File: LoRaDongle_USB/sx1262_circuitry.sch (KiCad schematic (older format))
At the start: 30 parts

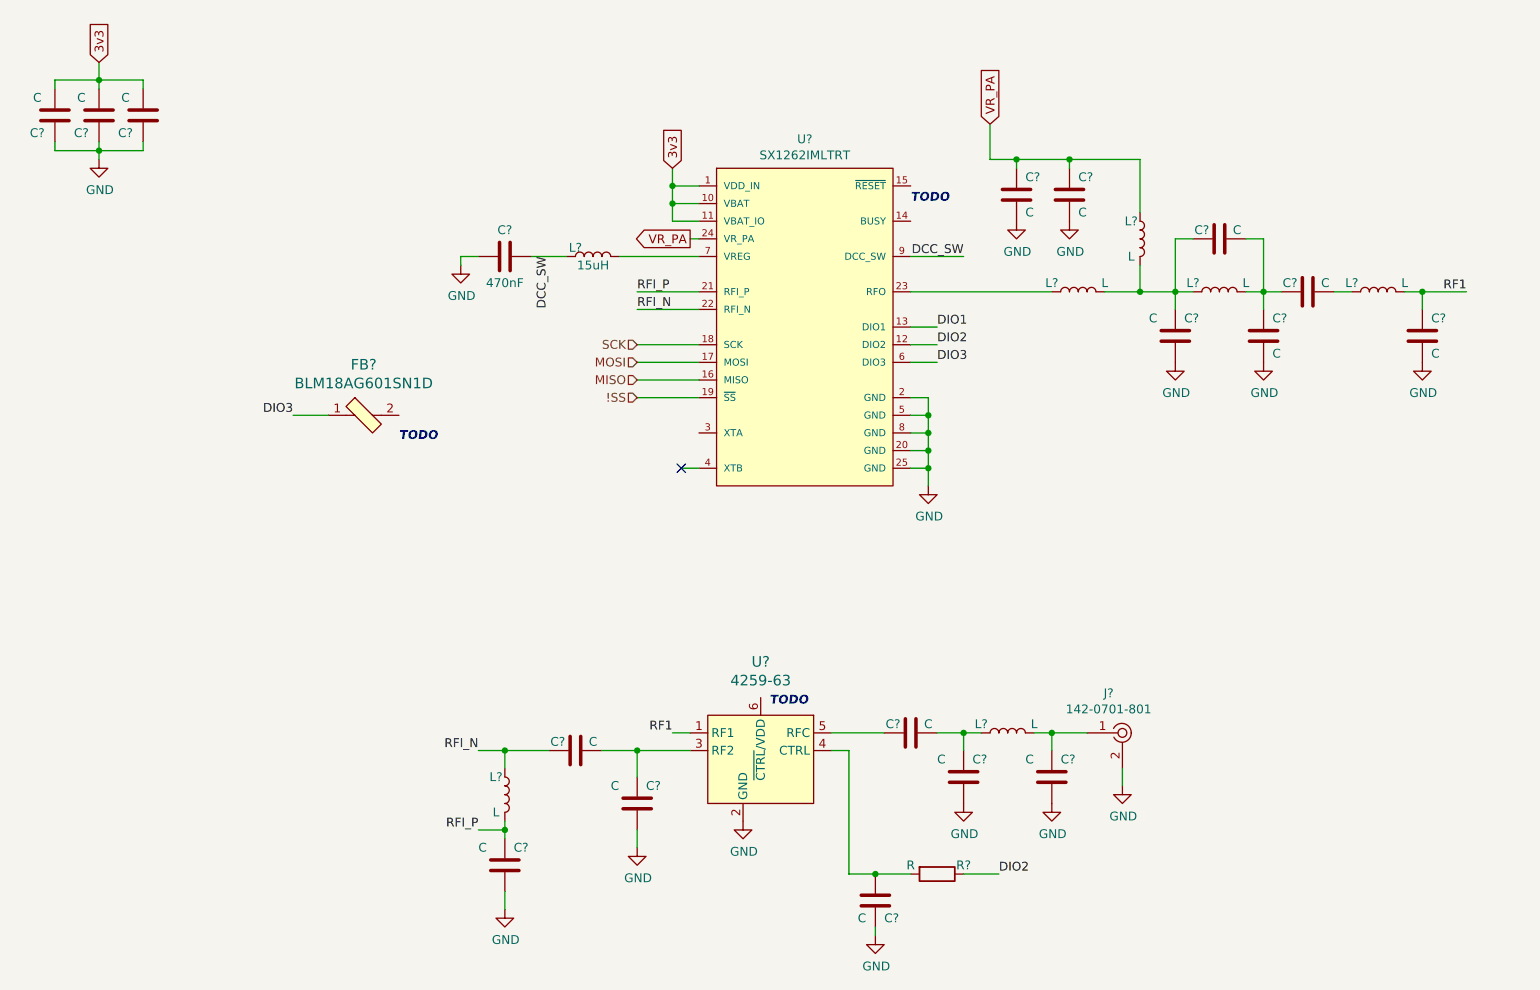
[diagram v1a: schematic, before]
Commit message: updated RF circuitry
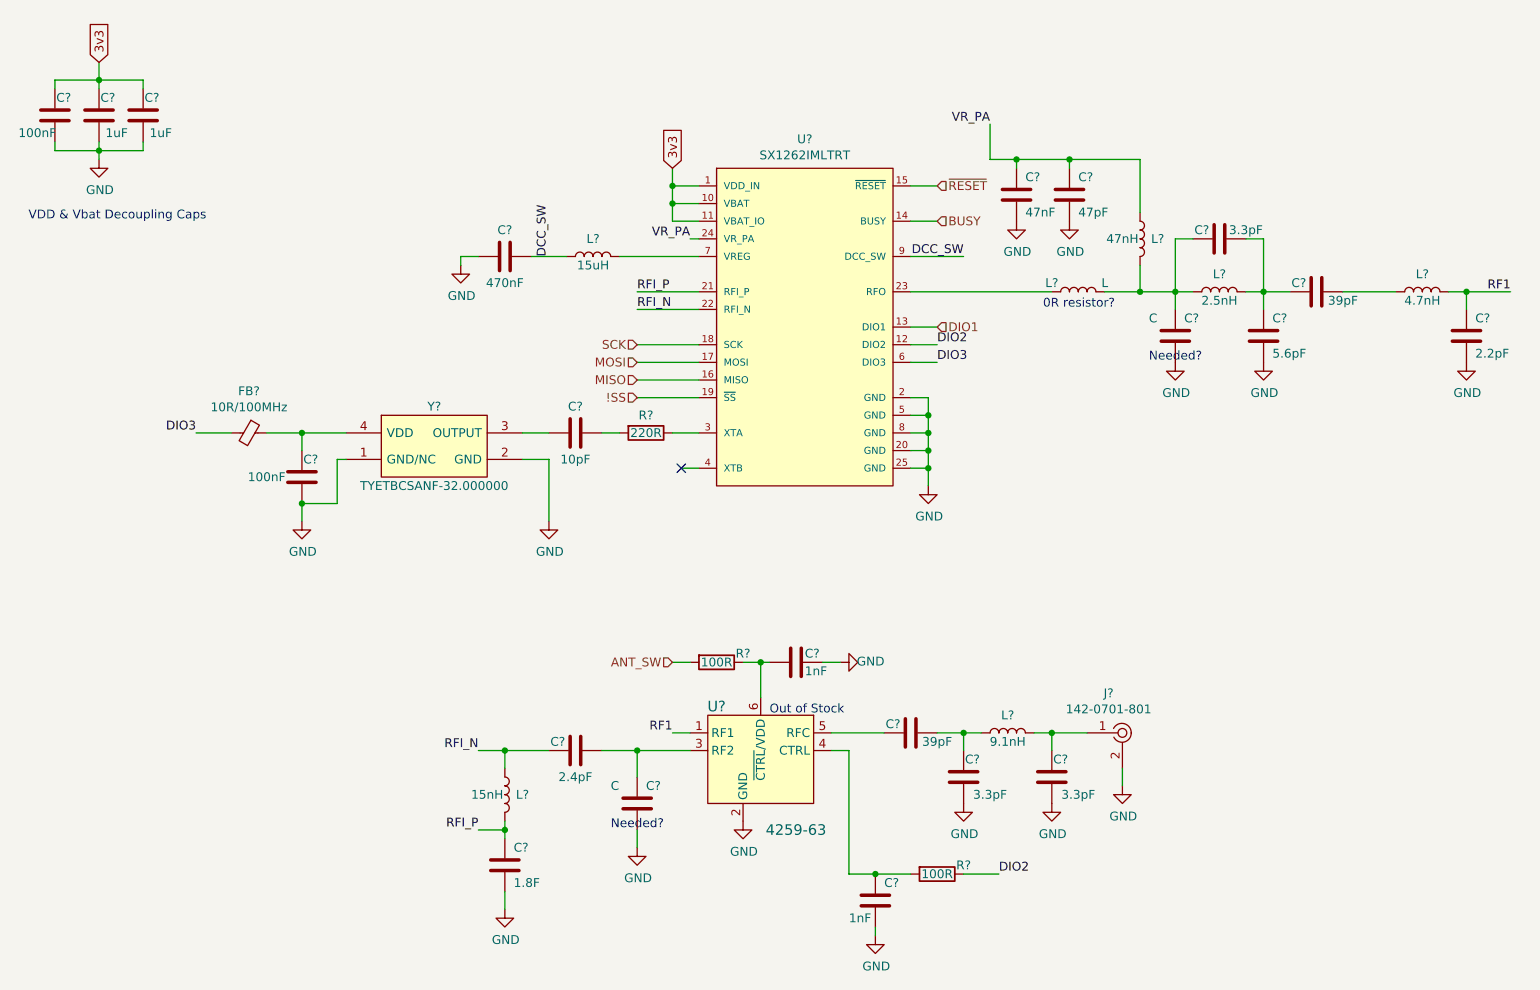
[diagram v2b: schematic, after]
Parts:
- removed C? (x4): C, symbol Device:C
- removed FB?: BLM18AG601SN1D, digikey-footprints:0603, symbol dk_Ferrite-Beads-and-Chips:BLM18AG601SN1D
- removed L?: 15uH, symbol Device:L
- removed R?: R, symbol Device:R
- added C? (x2): 3.3pF, Capacitor_SMD:C_0402_1005Metric, symbol Device:C
- added C?: 39pF, Capacitor_SMD:C_0402_1005Metric, symbol Device:C
- added C?: 1nF, Capacitor_SMD:C_0402_1005Metric, symbol Device:C
- added C?: 1uF, Capacitor_SMD:C_0402_1005Metric, symbol Device:C
- added C?: 100nF, Capacitor_SMD:C_0402_1005Metric, symbol Device:C
- added C?: 10pF, Capacitor_SMD:C_0402_1005Metric, symbol Device:C
- added FB?: 10R/100MHz, Inductor_SMD:L_0402_1005Metric, symbol Device:Ferrite_Bead_Small
- added L?: 15uH, VLS2016, symbol VLS201610CX-150M-1:VLS201610CX-150M-1
- added R? (x2): 100R, Resistor_SMD:R_0402_1005Metric, symbol Device:R
- added R?: 220R, Resistor_SMD:R_0402_1005Metric, symbol Device:R
- added Y?: TYETBCSANF-32.000000, TY, symbol TYETBCSANF-32.000000:TYETBCSANF-32.000000
- C?: value C -> 1nF; footprint (none) -> Capacitor_SMD:C_0402_1005Metric; Part Number (none) -> GRM155R72A102KA01D
- C?: value C -> 1.8F; footprint (none) -> Capacitor_SMD:C_0402_1005Metric; part Number (none) -> GRM1555C1H1R8BA01D
- C?: value C -> 2.4pF; footprint (none) -> Capacitor_SMD:C_0402_1005Metric; Part Number (none) -> GRM1555C1H2R4WA01D
- C?: value C -> 2.2pF; footprint (none) -> Capacitor_SMD:C_0402_1005Metric; Part Number (none) -> GRM1555C1H2R2BA01D
- C?: value C -> 39pF; footprint (none) -> Capacitor_SMD:C_0402_1005Metric; Part Number (none) -> GRM1555C1H390JA01D
- C?: value C -> 3.3pF; footprint (none) -> Capacitor_SMD:C_0402_1005Metric; Part Number (none) -> GJM1555C1H3R3DB01D
- C?: value C -> 5.6pF; footprint (none) -> Capacitor_SMD:C_0402_1005Metric; Part Number (none) -> GRM1555C1H5R6CA01J
- C?: value C -> 47pF; footprint (none) -> Capacitor_SMD:C_0402_1005Metric; Part Number (none) -> GRM1555C1H470JA01D
- C?: value C -> 47nF; footprint (none) -> Capacitor_SMD:C_0402_1005Metric; Part Number (none) -> GRM155R71C473KA01J
- C?: value C -> 1uF; footprint (none) -> Capacitor_SMD:C_0402_1005Metric; part Number (none) -> GRM188R61A105KA61D
- C?: value C -> 100nF; footprint (none) -> Capacitor_SMD:C_0402_1005Metric; Part Number (none) -> GRM155R71C104KA88D
- C?: footprint (none) -> Capacitor_SMD:C_0402_1005Metric; Part Number (none) -> GRM155R61A474KE15D
- L?: value L -> 15nH; footprint (none) -> Inductor_SMD:L_0402_1005Metric; part Number (none) -> LQW15AN15NH00D
- L?: value L -> 9.1nH; footprint (none) -> Inductor_SMD:L_0402_1005Metric; Part Number (none) -> LQW15AN9N1H00D
- L?: value L -> 4.7nH; footprint (none) -> Inductor_SMD:L_0402_1005Metric; Part Number (none) -> LQW15AN4N7C00D
- L?: value L -> 2.5nH; footprint (none) -> Inductor_SMD:L_0402_1005Metric; Part Number (none) -> LQW15AN2N5B00D
- L?: value L -> 47nH; footprint (none) -> Inductor_SMD:L_0402_1005Metric; Part Number (none) -> LQW15AN47NJ00D
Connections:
- net 3v3: now also C?.2
- net DCC_SW: now also L?.~
- net DIO2: now also R?.1
- net DIO3: now also FB?.2
- net GND: now also C?.1, C?.1, C?.1, C?.1, C?.1, Y?.1 (GND/NC), Y?.2 (GND)
- net at C?.1, U?.4 (CTRL): now also R?.2
- net at U?.5 (RFC): now also C?.2
- net at U?.6 (~CTRL~/VDD): now also C?.2, R?.1
- net at L?.1: now also C?.1, C?.2
- net at J?.1, L?.2: now also C?.2
- net at U?.7 (VREG): now also L?.~
- net BUSY: now reaches U?.14 (BUSY)
- net ~RESET: now reaches U?.15 (~RESET~)
- net at U?.3 (XTA): now also R?.1
- new net: C?.2, FB?.1, Y?.4 (VDD)
- new net: C?.2, Y?.3 (OUTPUT)
- new net: C?.1, R?.2
- new net ANT_SW: R?.2
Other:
- note added: "0R resistor?"
- note added: "Needed?\n"
- note added: "Out of Stock"
- note added: "VDD & Vbat Decoupling Caps"
- note removed: "TODO"
- moved on the sheet: C?, L?

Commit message: updated with dip switch
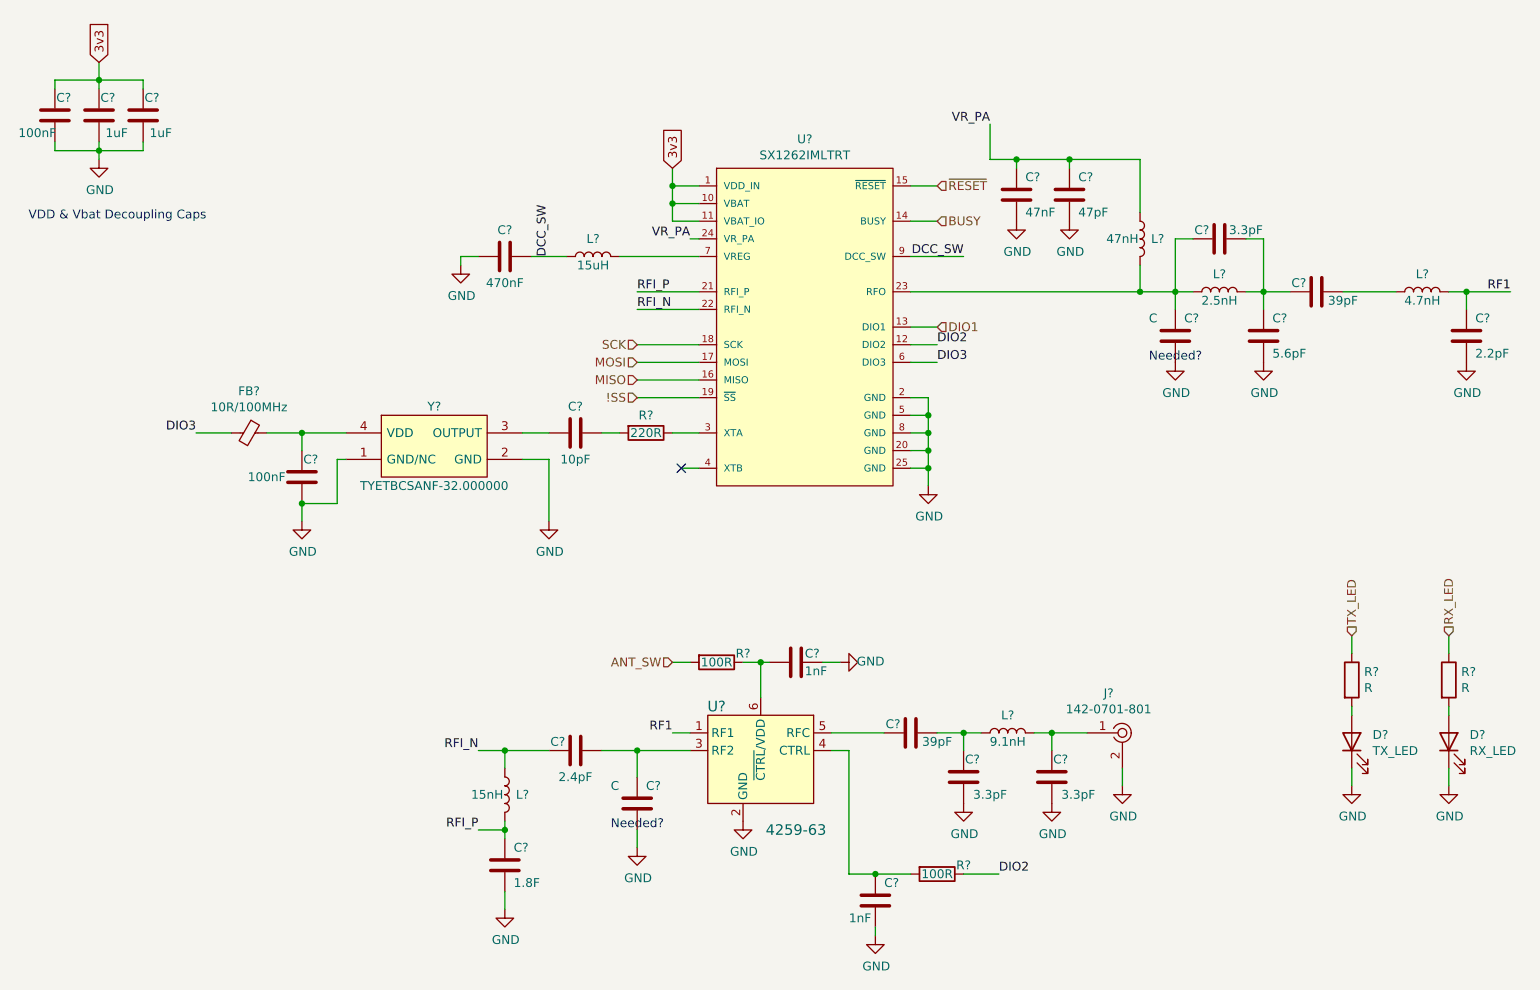
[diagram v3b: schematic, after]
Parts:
- removed L?: L, symbol Device:L
- added D?: TX_LED, symbol Device:LED
- added D?: RX_LED, symbol Device:LED
- added R? (x2): R, symbol Device:R
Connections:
- net GND: now also D?.1 (K), D?.1 (K)
- net at C?.1, C?.2, L?.1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: now also U?.23 (RFO)
- new net: D?.2 (A), R?.2 (x2)
- new net RX_LED: R?.1
- new net TX_LED: R?.1
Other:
- note removed: "0R resistor?"
- note removed: "Out of Stock"
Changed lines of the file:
@@
 $Descr A4 11693 8268
 encoding utf-8
-Sheet 6 7
+Sheet 7 7
 Title "LoRa Dongle"
 Date ""
@@
 Connection ~ 7600 2300
 Wire Wire Line
-	7600 2300 7400 2300
-Wire Wire Line
 	6750 1550 6900 1550
 Connection ~ 6900 1550
@@
 Wire Wire Line
 	5100 1800 4950 1800
-Wire Wire Line
-	6300 2300 7100 2300
-$Comp
-L Device:L L?
-U 1 1 6152F658
-P 7250 2300
-AR Path="/6152F658" Ref="L?"  Part="1"
-AR Path="/614F0720/6152F658" Ref="L?"  Part="1"
-F 0 "L?" V 7300 2450 50  0000 C CNN
-F 1 "L" V 7300 2150 50  0000 C CNN
-F 2 "" H 7250 2300 50  0001 C CNN
-F 3 "~" H 7250 2300 50  0001 C CNN
-	1    7250 2300
-	0    -1   -1   0
-$EndComp
 Wire Wire Line
 	4950 1800 4950 1700
@@
 	-1   0    0    1
 $EndComp
-Text Notes 7050 2400 0    50   ~ 0
-0R resistor?
 $Comp
 L VLS201610CX-150M-1:VLS201610CX-150M-1 L?
@@
 	0    1    1    0
 $EndComp
-Text Notes 5500 4700 0    50   ~ 0
-Out of Stock
 Text HLabel 6450 2500 2    50   Input ~ 0
 DIO1
+$Comp
+L Device:R R?
+U 1 1 61687A29
+P 8800 4500
+AR Path="/61687A29" Ref="R?"  Part="1"
+AR Path="/614F0720/61687A29" Ref="R?"  Part="1"
+F 0 "R?" H 8870 4546 50  0000 L CNN
+F 1 "R" H 8870 4455 50  0000 L CNN
+F 2 "" V 8730 4500 50  0001 C CNN
+F 3 "~" H 8800 4500 50  0001 C CNN
+	1    8800 4500
+	1    0    0    -1
+$EndComp
+$Comp
+L Device:LED D?
+U 1 1 61687A2F
+P 8800 4850
+AR Path="/61687A2F" Ref="D?"  Part="1"
+AR Path="/614F0720/61687A2F" Ref="D?"  Part="1"
+F 0 "D?" V 8839 4732 50  0000 R CNN
+F 1 "TX_LED" V 8748 4732 50  0000 R CNN
+F 2 "" H 8800 4850 50  0001 C CNN
+F 3 "~" H 8800 4850 50  0001 C CNN
+	1    8800 4850
+	0    -1   -1   0
+$EndComp
+$Comp
+L power:GND #PWR?
+U 1 1 61687A35
+P 8800 5100
+AR Path="/61687A35" Ref="#PWR?"  Part="1"
+AR Path="/614F0720/61687A35" Ref="#PWR?"  Part="1"
+F 0 "#PWR?" H 8800 4850 50  0001 C CNN
+F 1 "GND" H 8805 4927 50  0000 C CNN
+F 2 "" H 8800 5100 50  0001 C CNN
+F 3 "" H 8800 5100 50  0001 C CNN
+	1    8800 5100
+	1    0    0    -1
+$EndComp
+Wire Wire Line
+	8800 5100 8800 5000
+Wire Wire Line
+	8800 4700 8800 4650
+Wire Wire Line
+	8800 4350 8800 4250
+$Comp
+L Device:R R?
+U 1 1 6168CCFD
+P 9350 4500
+AR Path="/6168CCFD" Ref="R?"  Part="1"
+AR Path="/614F0720/6168CCFD" Ref="R?"  Part="1"
+F 0 "R?" H 9420 4546 50  0000 L CNN
+F 1 "R" H 9420 4455 50  0000 L CNN
+F 2 "" V 9280 4500 50  0001 C CNN
+F 3 "~" H 9350 4500 50  0001 C CNN
+	1    9350 4500
+	1    0    0    -1
+$EndComp
+$Comp
+L Device:LED D?
+U 1 1 6168CD03
+P 9350 4850
+AR Path="/6168CD03" Ref="D?"  Part="1"
+AR Path="/614F0720/6168CD03" Ref="D?"  Part="1"
+F 0 "D?" V 9389 4732 50  0000 R CNN
+F 1 "RX_LED" V 9298 4732 50  0000 R CNN
+F 2 "" H 9350 4850 50  0001 C CNN
+F 3 "~" H 9350 4850 50  0001 C CNN
+	1    9350 4850
+	0    -1   -1   0
+$EndComp
+$Comp
+L power:GND #PWR?
+U 1 1 6168CD09
+P 9350 5100
+AR Path="/6168CD09" Ref="#PWR?"  Part="1"
+AR Path="/614F0720/6168CD09" Ref="#PWR?"  Part="1"
+F 0 "#PWR?" H 9350 4850 50  0001 C CNN
+F 1 "GND" H 9355 4927 50  0000 C CNN
+F 2 "" H 9350 5100 50  0001 C CNN
+F 3 "" H 9350 5100 50  0001 C CNN
+	1    9350 5100
+	1    0    0    -1
+$EndComp
+Wire Wire Line
+	9350 5100 9350 5000
+Wire Wire Line
+	9350 4700 9350 4650
+Wire Wire Line
+	9350 4350 9350 4250
+Text HLabel 8800 4250 1    50   Input ~ 0
+TX_LED
+Text HLabel 9350 4250 1    50   Input ~ 0
+RX_LED
+Wire Wire Line
+	6300 2300 7600 2300
 $EndSCHEMATC
